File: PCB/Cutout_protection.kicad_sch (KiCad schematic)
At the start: 9 parts, among them K1 G5NB, Q2 MMBT3904, U6 LM358DR2G

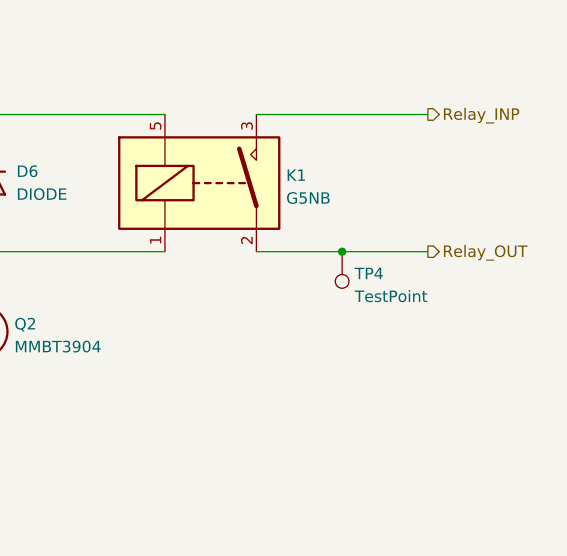
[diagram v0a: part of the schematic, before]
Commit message: Labelled Test Points
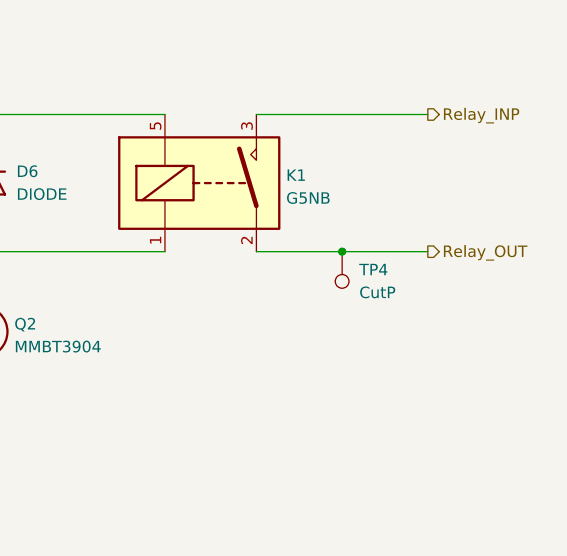
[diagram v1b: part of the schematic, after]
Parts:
- TP4: value TestPoint -> CutP
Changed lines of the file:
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@@
   (symbol (lib_id "Connector:TestPoint") (at 169.545 101.6 180) (unit 1)
     (in_bom yes) (on_board yes) (fields_autoplaced)
-    (property "Reference" "TP4" (id 0) (at 170.942 104.0673 0)
+    (property "Reference" "TP4" (id 0) (at 171.45 103.6319 0)
       (effects (font (size 1.27 1.27)) (justify right))
     )
-    (property "Value" "TestPoint" (id 1) (at 170.942 106.6042 0)
+    (property "Value" "CutP" (id 1) (at 171.45 106.1719 0)
       (effects (font (size 1.27 1.27)) (justify right))
     )
